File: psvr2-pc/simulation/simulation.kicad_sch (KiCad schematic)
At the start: 25 parts, among them Q1 PMOS, Q2 PMOS, Q3 NPN, Q4 PMOS, Q5 PMOS, Q6 NPN, Q8 PMOS

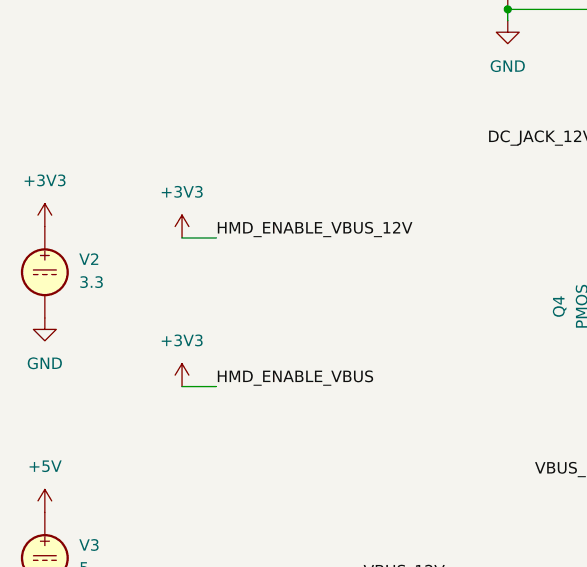
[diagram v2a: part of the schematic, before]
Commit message: Great, this doesn't work anymore after using the real library model. I'll need to see what's going on.
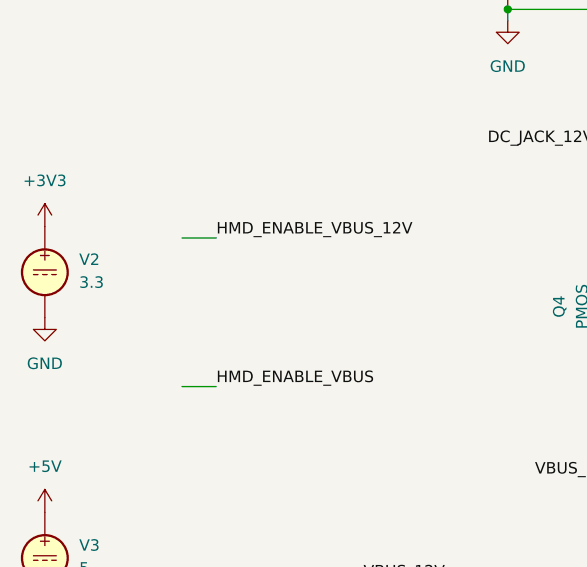
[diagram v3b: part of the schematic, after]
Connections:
- net +3V3: no longer R11.2, R12.2, R5.2, R6.2
- new net HMD_ENABLE_VBUS: R11.2, R12.2
- new net HMD_ENABLE_VBUS_12V: R5.2, R6.2
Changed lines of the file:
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@@
-	)
-	(symbol
-		(lib_id "power:+3V3")
-		(at 36.83 73.66 0)
-		(unit 1)
-		(exclude_from_sim no)
-		(in_bom yes)
-		(on_board yes)
-		(dnp no)
-		(fields_autoplaced yes)
-		(property "Reference" "#PWR018"
-			(at 36.83 77.47 0)
-			(effects
-				(font
-					(size 1.27 1.27)
-				)
-				(hide yes)
-			)
-		)
-		(property "Value" "+3V3"
-			(at 36.83 68.58 0)
-			(effects
-				(font
-					(size 1.27 1.27)
-				)
-			)
-		)
-		(property "Footprint" ""
-			(at 36.83 73.66 0)
-			(effects
-				(font
-					(size 1.27 1.27)
-				)
-				(hide yes)
-			)
-		)
-		(property "Datasheet" ""
-			(at 36.83 73.66 0)
-			(effects
-				(font
-					(size 1.27 1.27)
-				)
-				(hide yes)
-			)
-		)
-		(property "Description" "Power symbol creates a global label with name \"+3V3\""
-			(at 36.83 73.66 0)
-			(effects
-				(font
-					(size 1.27 1.27)
-				)
-				(hide yes)
-			)
-		)
-		(pin "1"
-		)
-		(instances
-			(project "simulation"
-				(path "/f11bb3d3-5794-4a95-b9a9-d0bd9f1c0d65"
-					(reference "#PWR018")
-					(unit 1)
-				)
-			)
-		)
 	)
 	(symbol
@@
 			)
 		)
-		(property "Sim.Device" "PMOS"
+		(property "Sim.Device" "SUBCKT"
 			(at 106.68 116.205 0)
-			(effects
-				(font
-					(size 1.27 1.27)
-				)
-				(hide yes)
-			)
-		)
-		(property "Sim.Type" "VDMOS"
-			(at 106.68 114.3 0)
 			(effects
 				(font
@@
 			)
 		)
+		(property "Sim.Library" "C:\\Users\\Usuario\\Downloads\\si2301cds_ps_revb\\si2301cds_ps Rev B.lib"
+			(at 106.68 133.35 0)
+			(effects
+				(font
+					(size 1.27 1.27)
+				)
+				(hide yes)
+			)
+		)
+		(property "Sim.Name" "Si2301CDS"
+			(at 106.68 133.35 0)
+			(effects
+				(font
+					(size 1.27 1.27)
+				)
+				(hide yes)
+			)
+		)
 		(pin "2"
 		)
@@
 			)
 		)
-		(property "Sim.Device" "PMOS"
+		(property "Sim.Device" "SUBCKT"
 			(at 109.855 97.79 0)
-			(effects
-				(font
-					(size 1.27 1.27)
-				)
-				(hide yes)
-			)
-		)
-		(property "Sim.Type" "VDMOS"
-			(at 111.76 97.79 0)
 			(effects
 				(font
@@
 		(property "Sim.Pins" "1=D 2=G 3=S"
 			(at 107.95 97.79 0)
+			(effects
+				(font
+					(size 1.27 1.27)
+				)
+				(hide yes)
+			)
+		)
+		(property "Sim.Library" "C:\\Users\\Usuario\\Downloads\\si2301cds_ps_revb\\si2301cds_ps Rev B.lib"
+			(at 92.71 97.79 90)
+			(effects
+				(font
+					(size 1.27 1.27)
+				)
+				(hide yes)
+			)
+		)
+		(property "Sim.Name" "Si2301CDS"
+			(at 92.71 97.79 0)
 			(effects
 				(font
@@
 			)
 		)
-		(property "Sim.Device" "PMOS"
+		(property "Sim.Device" "SUBCKT"
 			(at 87.63 47.625 0)
-			(effects
-				(font
-					(size 1.27 1.27)
-				)
-				(hide yes)
-			)
-		)
-		(property "Sim.Type" "VDMOS"
-			(at 87.63 45.72 0)
 			(effects
 				(font
@@
 		(property "Sim.Pins" "1=D 2=G 3=S"
 			(at 87.63 49.53 0)
+			(effects
+				(font
+					(size 1.27 1.27)
+				)
+				(hide yes)
+			)
+		)
+		(property "Sim.Library" "C:\\Users\\Usuario\\Downloads\\si2301cds_ps_revb\\si2301cds_ps Rev B.lib"
+			(at 87.63 64.77 0)
+			(effects
+				(font
+					(size 1.27 1.27)
+				)
+				(hide yes)
+			)
+		)
+		(property "Sim.Name" "Si2301CDS"
+			(at 87.63 64.77 0)
 			(effects
 				(font
@@
 			)
 		)
-		(property "Sim.Device" "NPN"
+		(property "Sim.Device" "SUBCKT"
 			(at 139.7 146.05 0)
 			(effects
@@
 			)
 		)
-		(property "Sim.Type" "GUMMELPOON"
+		(property "Sim.Pins" "1=D 2=G 3=S"
 			(at 139.7 146.05 0)
 			(effects
@@
 			)
 		)
-		(property "Sim.Pins" "1=C 2=B 3=E"
+		(property "Sim.Library" "C:\\Users\\Usuario\\Downloads\\si2301cds_ps_revb\\si2301cds_ps Rev B.lib"
+			(at 139.7 146.05 0)
+			(effects
+				(font
+					(size 1.27 1.27)
+				)
+				(hide yes)
+			)
+		)
+		(property "Sim.Name" "Si2301CDS"
 			(at 139.7 146.05 0)
 			(effects
@@
 	)
 	(symbol
-		(lib_id "power:+3V3")
-		(at 36.83 57.15 0)
-		(unit 1)
-		(exclude_from_sim no)
-		(in_bom yes)
-		(on_board yes)
-		(dnp no)
-		(fields_autoplaced yes)
-		(property "Reference" "#PWR017"
-			(at 36.83 60.96 0)
-			(effects
-				(font
-					(size 1.27 1.27)
-				)
-				(hide yes)
-			)
-		)
-		(property "Value" "+3V3"
-			(at 36.83 52.07 0)
-			(effects
-				(font
-					(size 1.27 1.27)
-				)
-			)
-		)
-		(property "Footprint" ""
-			(at 36.83 57.15 0)
-			(effects
-				(font
-					(size 1.27 1.27)
-				)
-				(hide yes)
-			)
-		)
-		(property "Datasheet" ""
-			(at 36.83 57.15 0)
-			(effects
-				(font
-					(size 1.27 1.27)
-				)
-				(hide yes)
-			)
-		)
-		(property "Description" "Power symbol creates a global label with name \"+3V3\""
-			(at 36.83 57.15 0)
-			(effects
-				(font
-					(size 1.27 1.27)
-				)
-				(hide yes)
-			)
-		)
-		(pin "1"
-		)
-		(instances
-			(project "simulation"
-				(path "/f11bb3d3-5794-4a95-b9a9-d0bd9f1c0d65"
-					(reference "#PWR017")
-					(unit 1)
-				)
-			)
-		)
-	)
-	(symbol
 		(lib_id "Device:R_Small")
 		(at 68.58 98.425 0)
@@
 			)
 		)
-		(property "Sim.Device" "PMOS"
+		(property "Sim.Device" "SUBCKT"
 			(at 116.205 24.13 0)
-			(effects
-				(font
-					(size 1.27 1.27)
-				)
-				(hide yes)
-			)
-		)
-		(property "Sim.Type" "VDMOS"
-			(at 118.11 24.13 0)
 			(effects
 				(font
@@
 		(property "Sim.Pins" "1=D 2=G 3=S"
 			(at 114.3 24.13 0)
+			(effects
+				(font
+					(size 1.27 1.27)
+				)
+				(hide yes)
+			)
+		)
+		(property "Sim.Library" "C:\\Users\\Usuario\\Downloads\\si2301cds_ps_revb\\si2301cds_ps Rev B.lib"
+			(at 99.06 24.13 0)
+			(effects
+				(font
+					(size 1.27 1.27)
+				)
+				(hide yes)
+			)
+		)
+		(property "Sim.Name" "Si2301CDS"
+			(at 99.06 24.13 0)
 			(effects
 				(font
@@
 			)
 		)
-		(property "Sim.Device" "PMOS"
+		(property "Sim.Device" "SUBCKT"
 			(at 109.855 110.49 0)
-			(effects
-				(font
-					(size 1.27 1.27)
-				)
-				(hide yes)
-			)
-		)
-		(property "Sim.Type" "VDMOS"
-			(at 111.76 110.49 0)
 			(effects
 				(font
@@
 			(effects
 				(font
+					(size 1.27 1.27)
+				)
+				(hide yes)
+			)
+		)
+		(property "Sim.Library" "C:\\Users\\Usuario\\Downloads\\si2301cds_ps_revb\\si2301cds_ps Rev B.lib"
+			(at 92.71 110.49 0)
+			(effects
+				(font
+					(size 1.27 1.27)
+				)
+				(hide yes)
+			)
+		)
+		(property "Sim.Name" "Si2301CDS"
+			(at 92.71 110.49 0)
+			(effects
+				(font

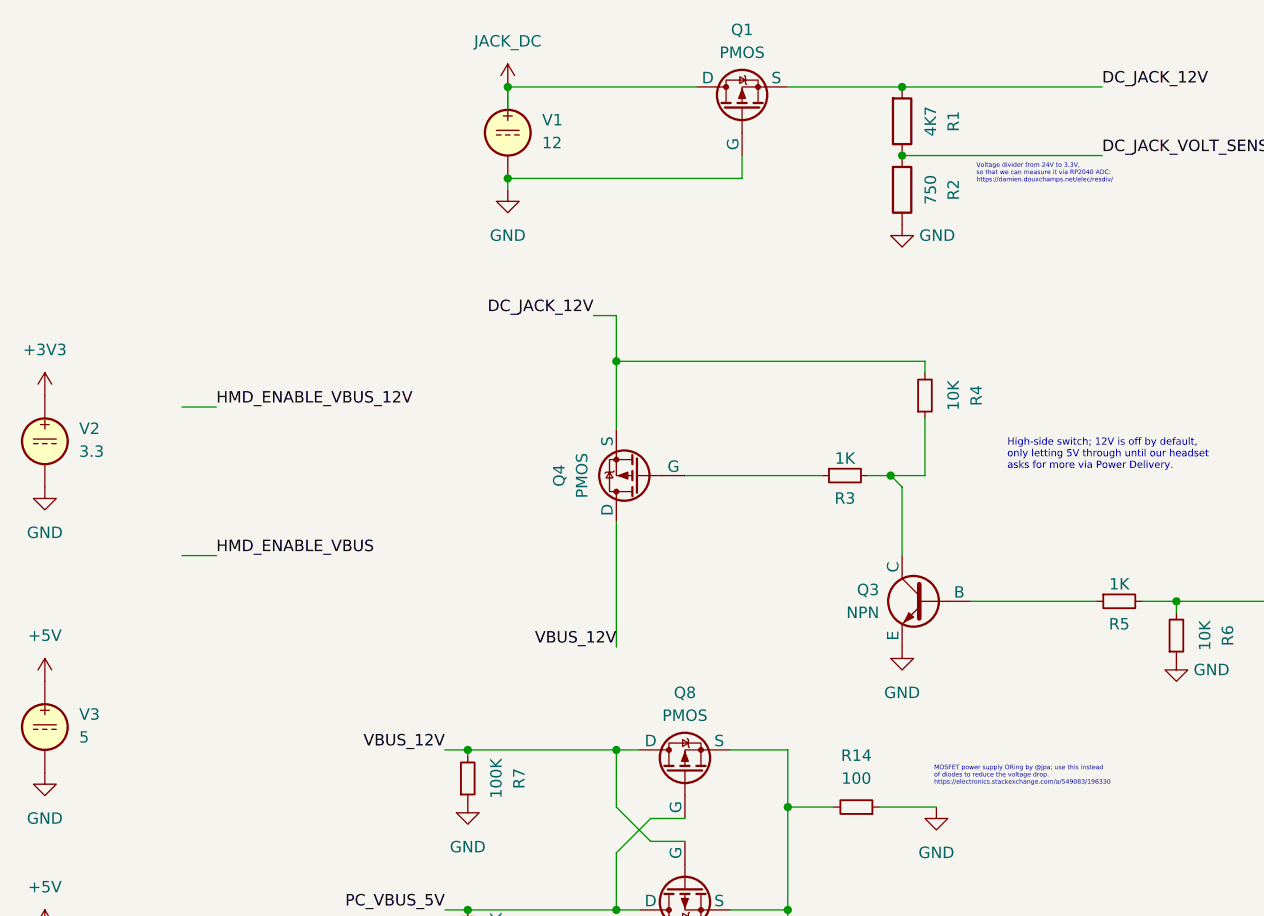
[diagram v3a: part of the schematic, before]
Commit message: Welp, using the actual model library file it stops working, great. If the P-MOSFET is on it works properly, but when off there seems to be a problem with the diode clamping it to 2.60V. I don't know if the model is wrong or I'm using the wrong component. Replaced this one (si2301cds_ps Rev B.lib) with an AO3401A and seems to work fine.
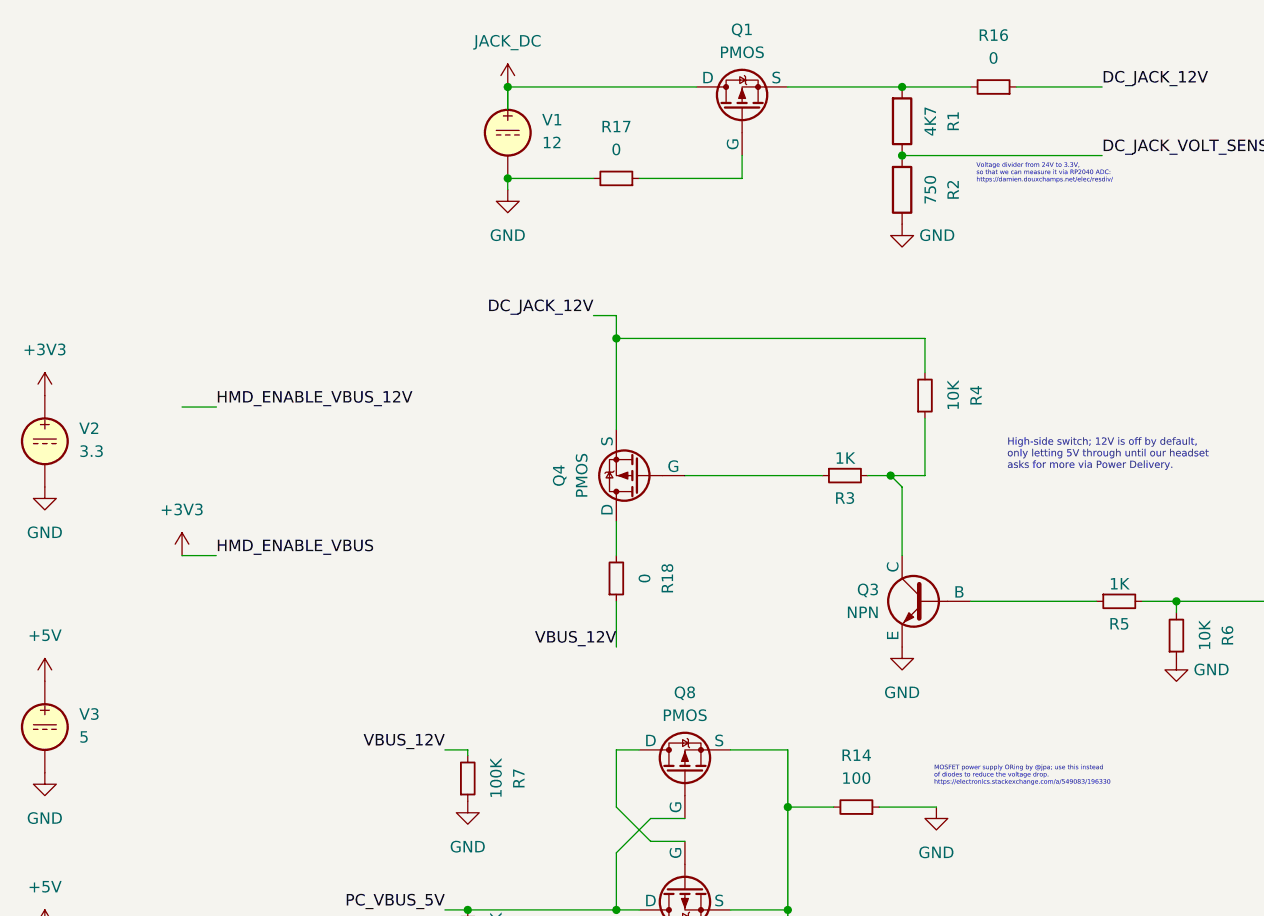
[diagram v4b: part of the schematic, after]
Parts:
- added R16, R17, R18: 0, Resistor_SMD:R_0805_2012Metric, symbol Device:R_Small
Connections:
- net HMD_ENABLE_VBUS is gone; now on net +3V3: R11.2, R12.2
- net DC_JACK_12V: now also R16.1; no longer Q1.3 (S), R1.2
- net GND: now also R17.2; no longer Q1.2 (G)
- net VBUS_12V: now also R18.1; no longer Q2.2 (G), Q4.1 (D), Q8.1 (D)
- new net: Q4.1 (D), R18.2
- new net: Q2.2 (G), Q8.1 (D)
- new net: Q1.3 (S), R1.2, R16.2
- new net: Q1.2 (G), R17.1

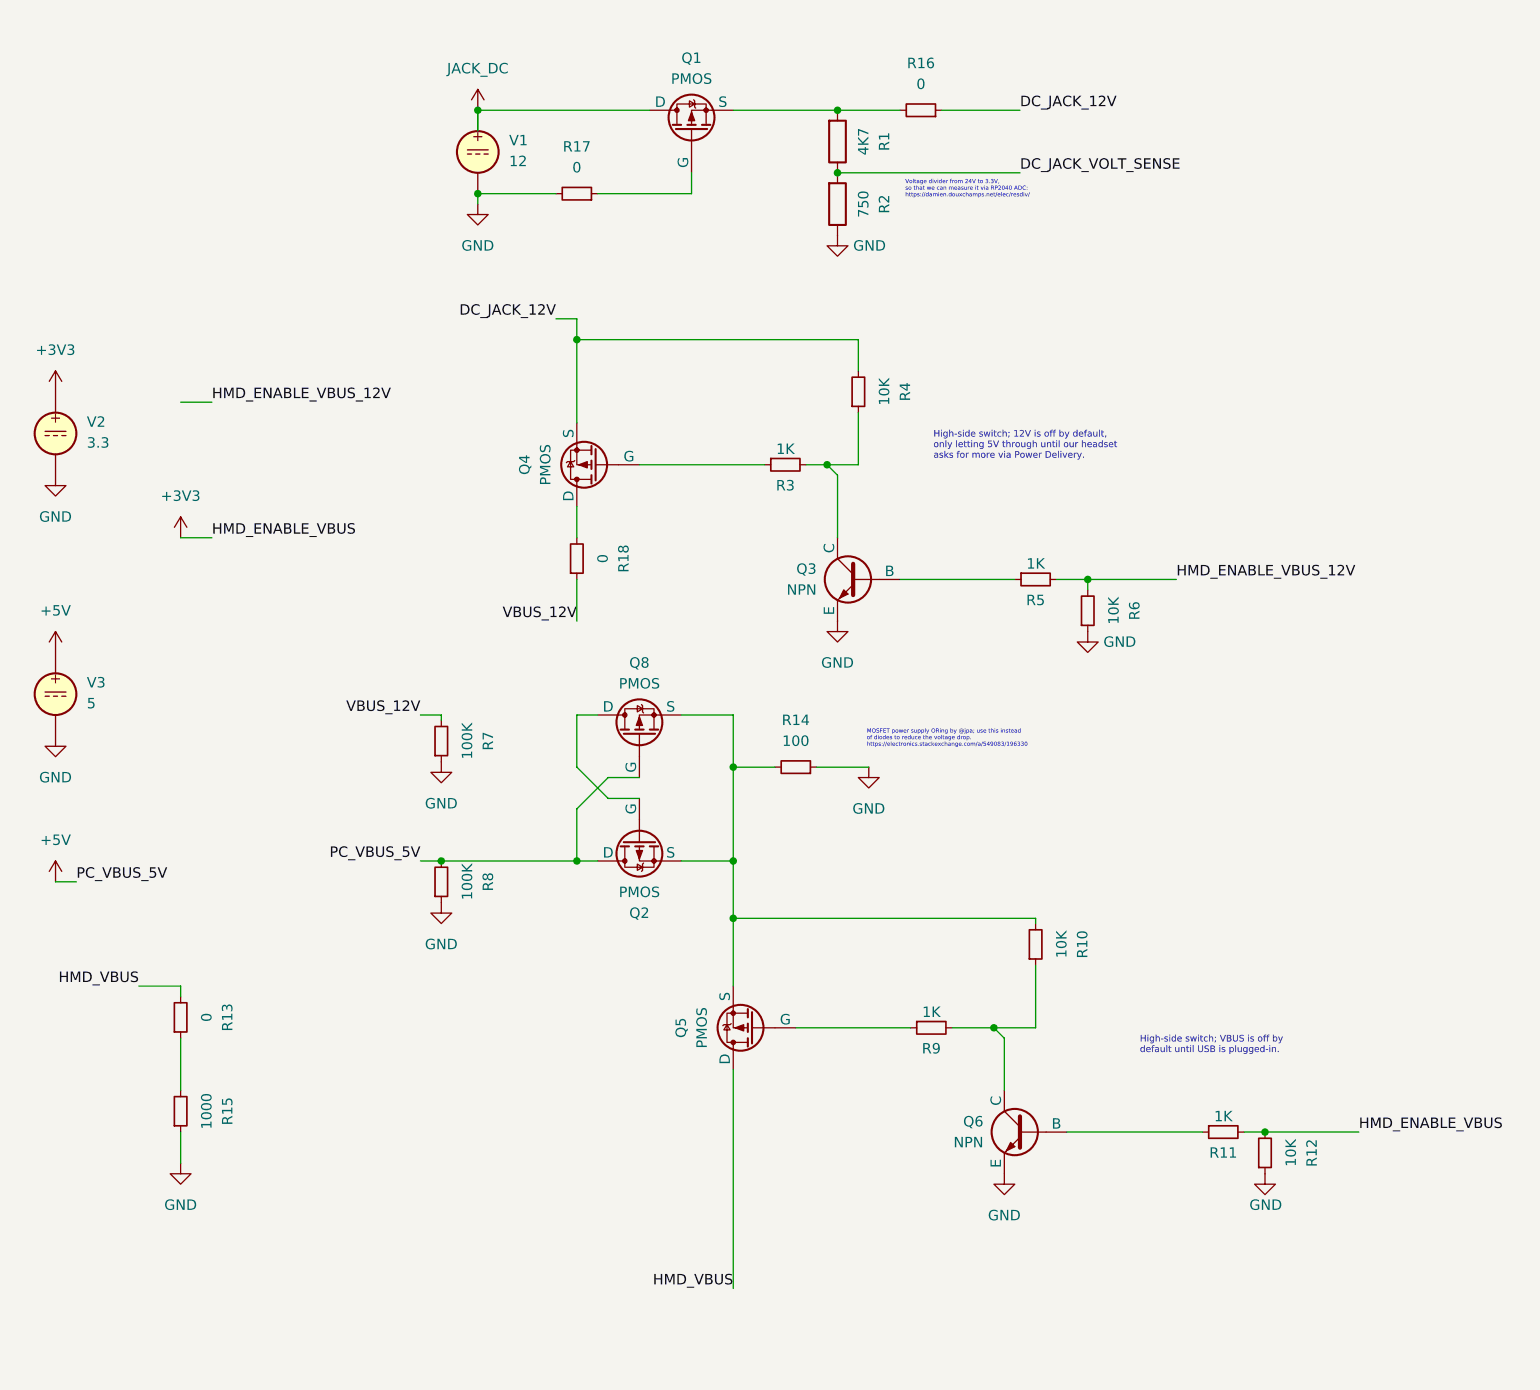
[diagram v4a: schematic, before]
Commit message: I know why the simulation didn't work; I applied the P-MOSFET model to the Q6/HMD_ENABLE_BUS NPN transistor. I'm stupid, as usual. :)
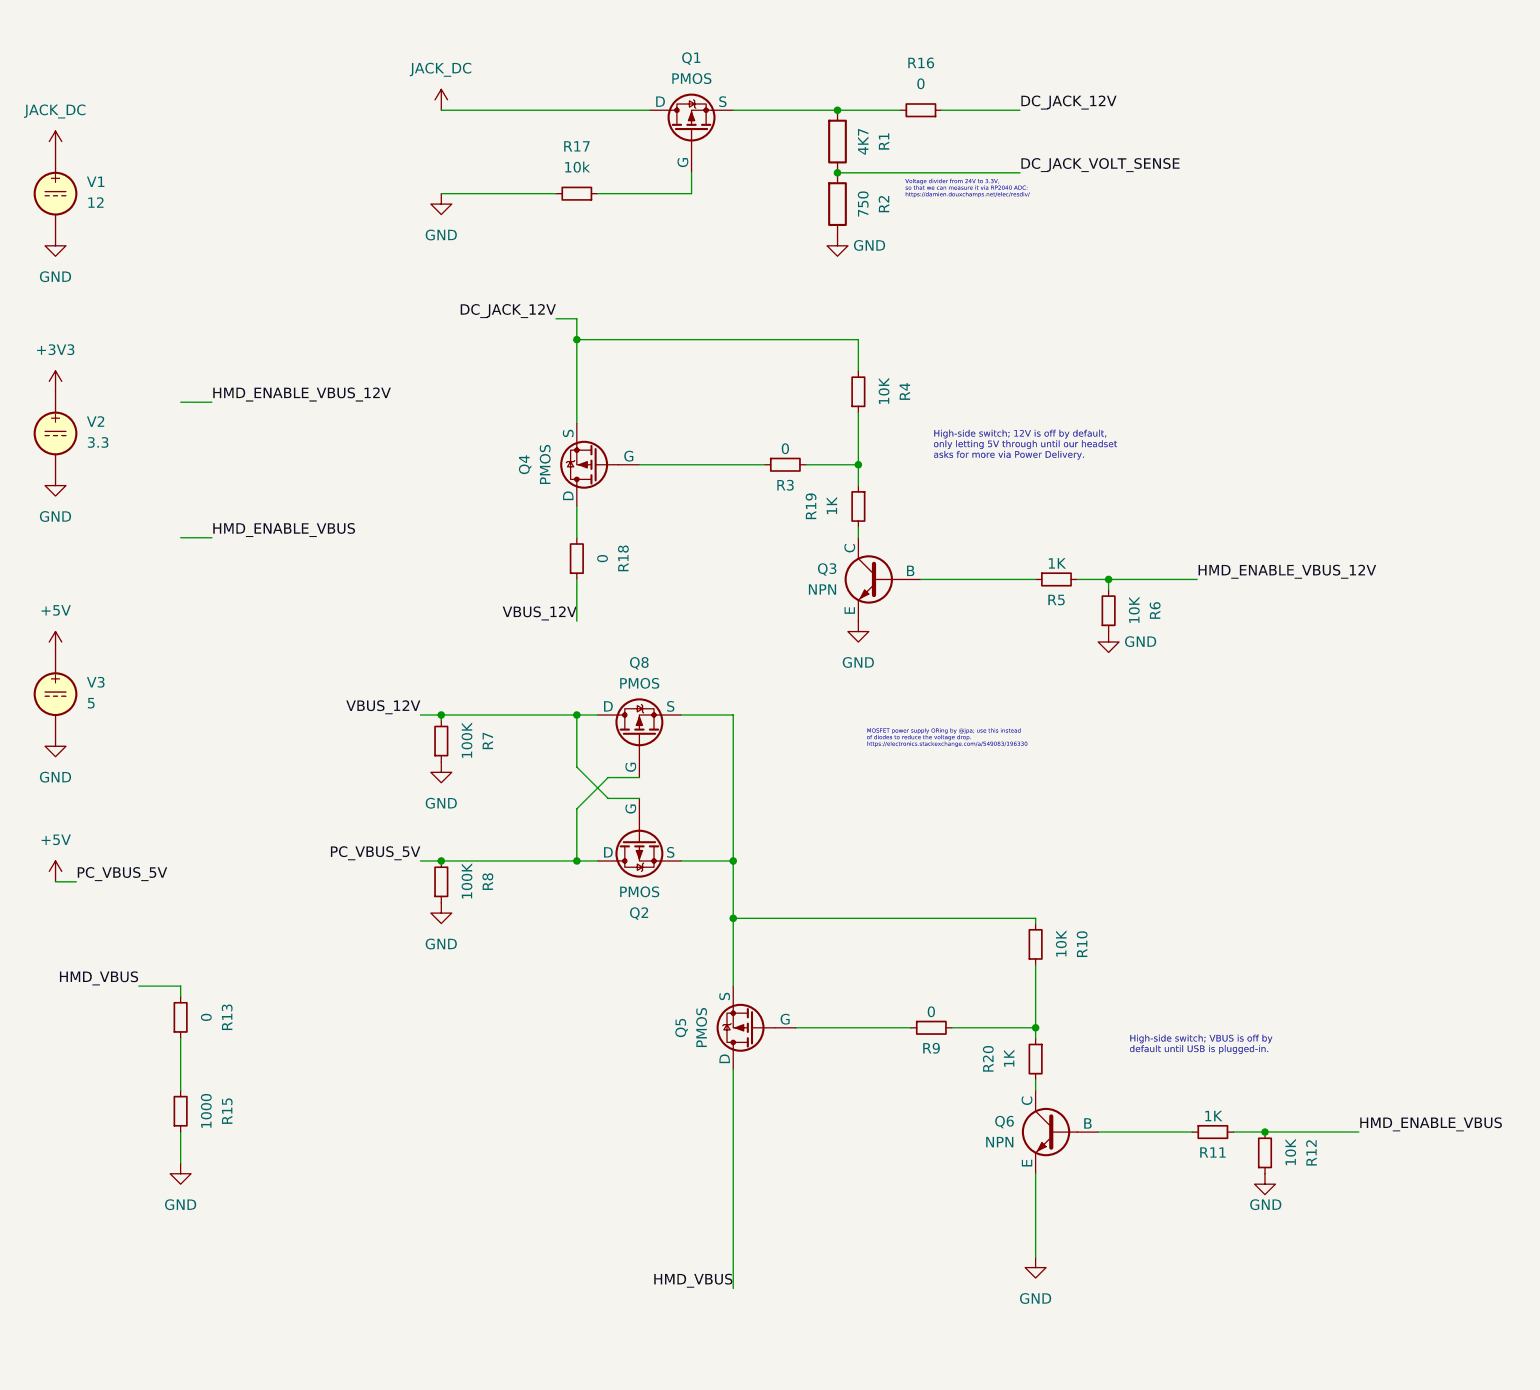
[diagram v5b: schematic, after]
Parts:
- removed R14: 100, Resistor_SMD:R_0805_2012Metric, symbol Device:R_Small
- added R19, R20: 1K, Resistor_SMD:R_0805_2012Metric, symbol Device:R_Small
- R17: value 0 -> 10k
- R3, R9: value 1K -> 0
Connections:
- net +3V3: no longer R11.2, R12.2
- net VBUS_12V: now also Q2.2 (G), Q8.1 (D)
- net at R10.1, R9.2: now also R20.1; no longer Q6.1 (C)
- net at R3.2, R4.1: now also R19.1; no longer Q3.1 (C)
- new net: Q6.1 (C), R20.2
- new net: Q3.1 (C), R19.2
- new net HMD_ENABLE_VBUS: R11.2, R12.2
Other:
- moved on the sheet: Q3, Q6, R11, R5, R6
